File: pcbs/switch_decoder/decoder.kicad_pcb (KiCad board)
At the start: 2 copper layers, 97.5 x 67.1 mm, 70 parts, among them J1 Screw_Terminal_01x06, J2 AVR-ISP-6, J3 Screw_Terminal_01x06, J4 RJ45_LED_Shielded, J5 RJ45_LED_Shielded, Q1 2N7002, Q10 2N7002, Q11 2N7002, Q12 2N7002, Q13 2N7002, Q2 2N7002, Q3 2N7002, Q4 2N7002, Q5 2N7002, Q6 2N7002, Q7 2N7002, Q8 2N7002, Q9 2N7002, SW1 SW_DIP_x06, U1 ATmega328P-AU, U10 74HC595, U2 74HC595, U3 MIC4427, U4 MAX481E, U5 MIC4427, U6 MIC4427, U7 MIC4427, U8 MIC4427, U9 MIC4427, Y1 16MHz

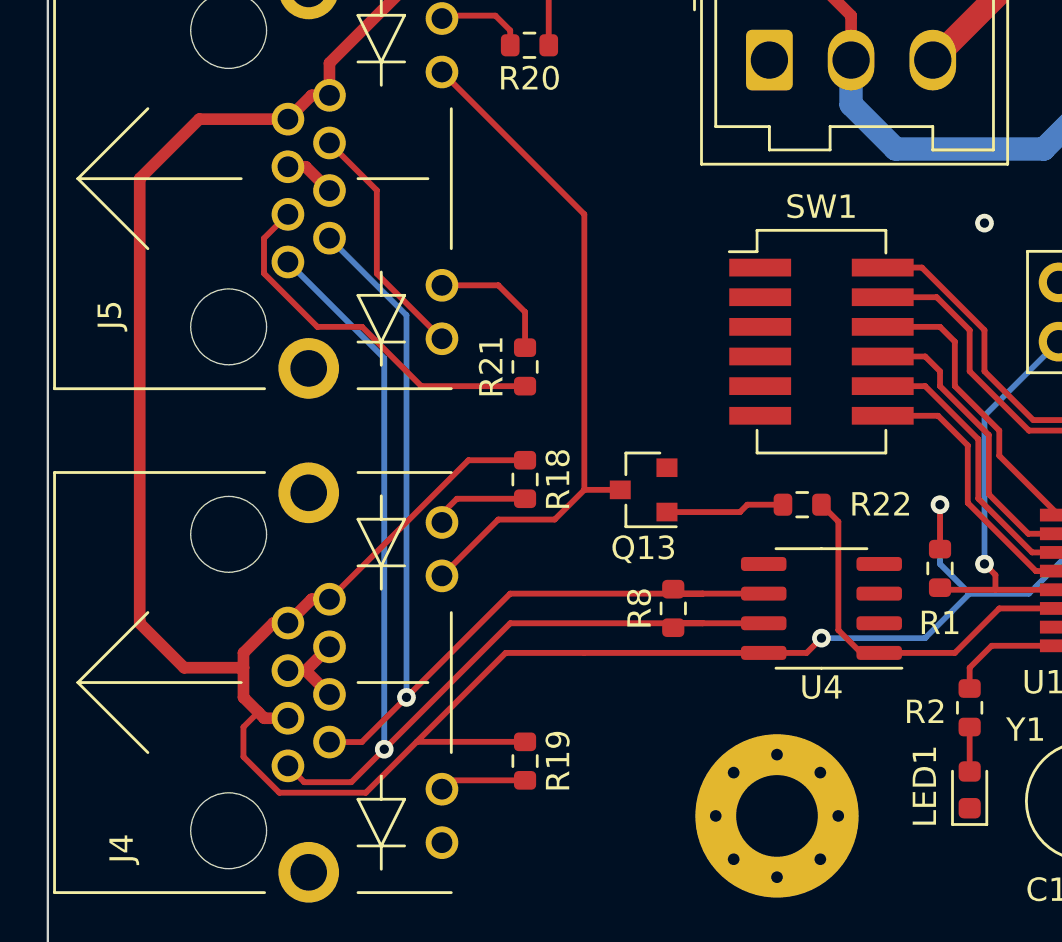
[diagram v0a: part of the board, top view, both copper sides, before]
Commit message: produced PCBs, dropped baudrate, removed on-board dynamic address selection - decoder must now be configured via programmer!
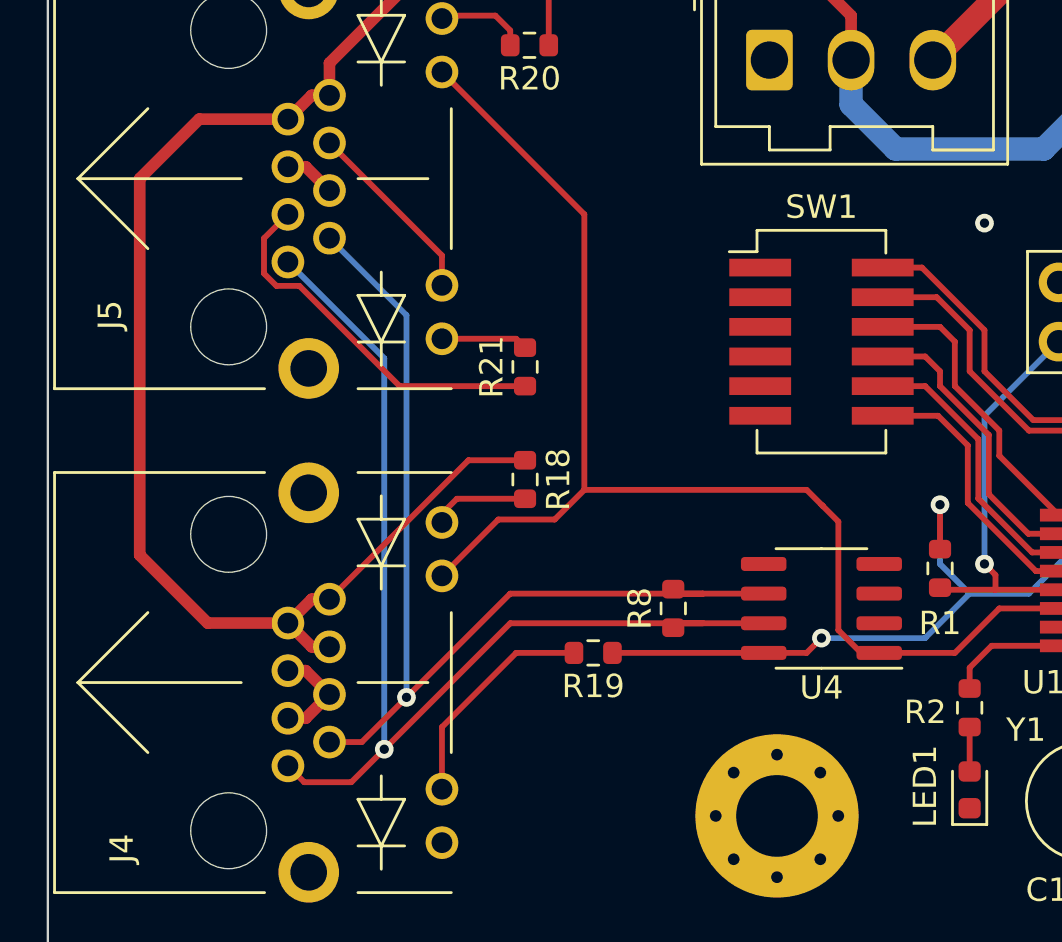
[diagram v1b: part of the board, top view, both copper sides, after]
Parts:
- removed Q13: 2N7002, Package_TO_SOT_SMD:SOT-23
- removed R22: 1k, Resistor_SMD:R_0603_1608Metric
- moved R19 5.48 mm to (116.6, 100.3), turned to 180 degrees
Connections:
- net /networking/A+ renamed Net-(J4-Pad1)
- net /networking/A- renamed Net-(J4-Pad2)
- J4 pad 11: Net-(J4-Pad11) -> /networking/Rx
- J4 pad 3: 5V -> GND
- J4 pad 6: GND -> 5V
- J5 pad 11: Net-(J4-Pad11) -> /networking/Rx
- J5 pad 6: Net-(J5-Pad6) -> Net-(J5-Pad10)
- J5 pad 9: Net-(J5-Pad6) -> Net-(J5-Pad9)
- R21 pad 2: Net-(J5-Pad10) -> Net-(J5-Pad9)
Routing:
- net /networking/Rx: track 16.3 -> 54.9 mm
- net 5V: track 362.4 -> 331.7 mm
- net Net-(J4-Pad11): track 29.6 -> 0.00 mm
- net Net-(J5-Pad6): track 10.4 -> 0.00 mm
- net Net-(J4-Pad10): track 3.72 -> 9.63 mm
- net Net-(Q13-Pad1): track 5.10 -> 0.00 mm
- net Net-(J5-Pad9): track 0.00 -> 3.72 mm
- net Net-(J5-Pad10): track 5.56 -> 8.10 mm
- net GND: track 223.0 -> 223.7 mm

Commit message: revision b of boards
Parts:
- C3: footprint Capacitor_THT:C_Radial_D8.0mm_H11.5mm_P3.50mm -> Capacitor_THT:CP_Radial_D8.0mm_P3.50mm
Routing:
- net /switch 1/Out_1: track 16.5 -> 19.1 mm
